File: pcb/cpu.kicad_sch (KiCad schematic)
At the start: 14 parts, among them J9 CLKMUL SET, U1 486Socket

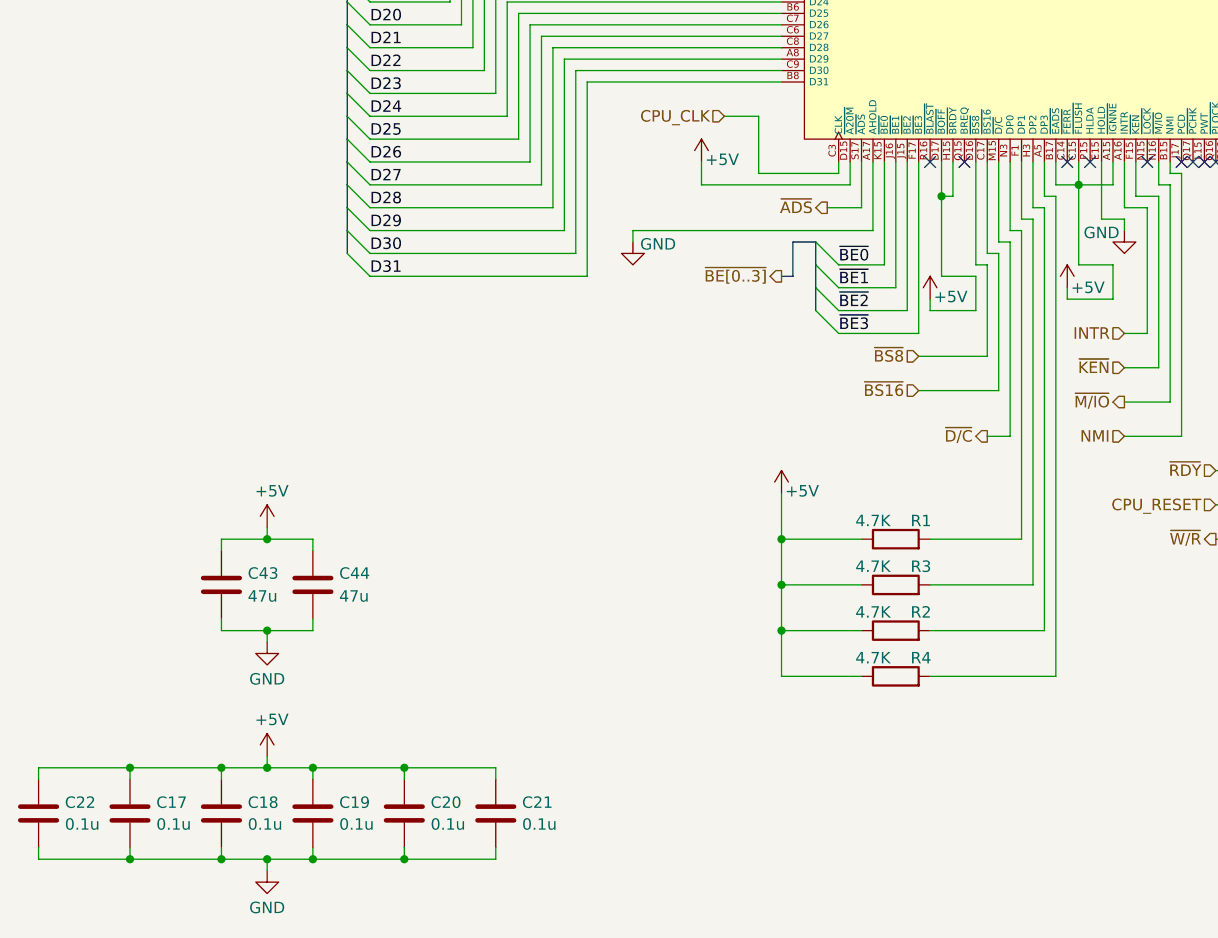
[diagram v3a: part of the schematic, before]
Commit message: cpu DPx use Resistor Array instead of individual resistors
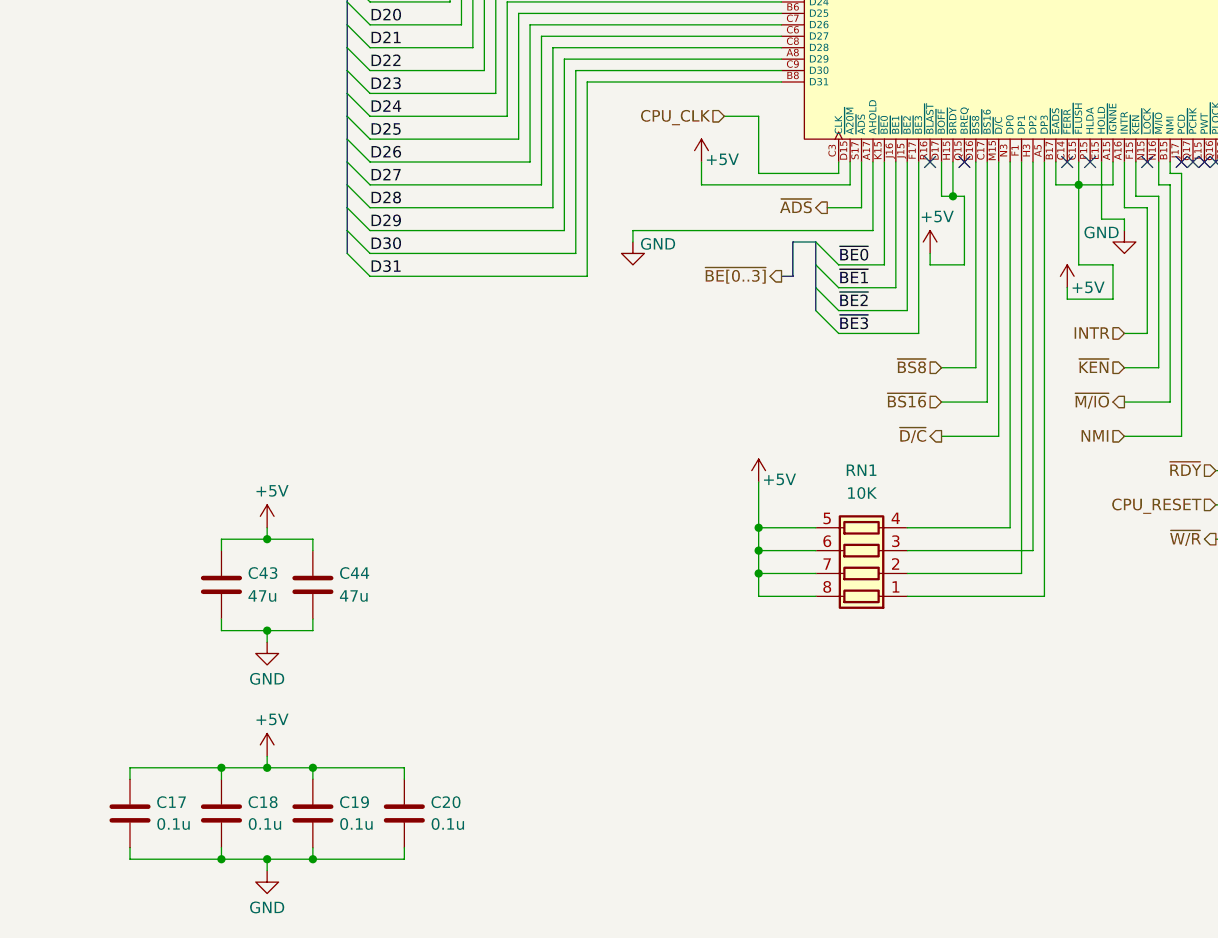
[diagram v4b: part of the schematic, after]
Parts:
- removed C21, C22: 0.1u, Capacitor_SMD:C_0805_2012Metric_Pad1.18x1.45mm_HandSolder, symbol Device:C
- removed R1, R2, R3, R4: 4.7K, Resistor_SMD:R_0805_2012Metric_Pad1.20x1.40mm_HandSolder, symbol Device:R
- added RN1: 10K, Resistor_SMD:R_Array_Convex_4x1206, symbol Device:R_Pack04
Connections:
- net +5V: now also RN1.5 (R4.2), RN1.6 (R3.2), RN1.7 (R2.2), RN1.8 (R1.2)
- net at U1.N3 (DP0): now also RN1.4 (R4.1)
- net at U1.A5 (DP3): now also RN1.1 (R1.1)
- net at U1.F1 (DP1): now also RN1.2 (R2.1)
- net at U1.H3 (DP2): now also RN1.3 (R3.1)

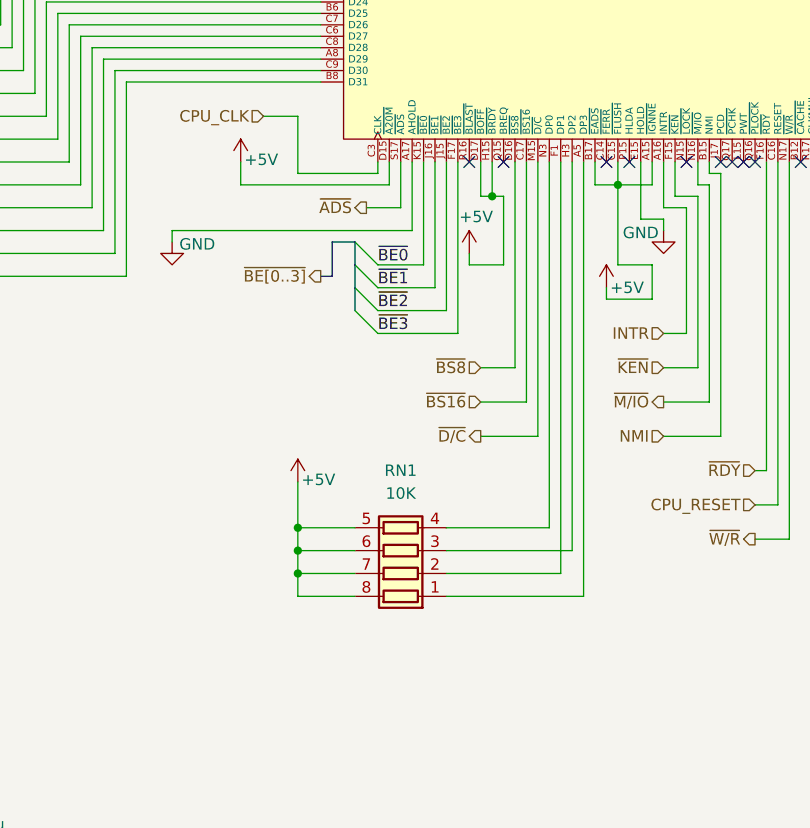
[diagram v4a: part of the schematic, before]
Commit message: cpu added convenient test point on BRDY near RDY for optional link
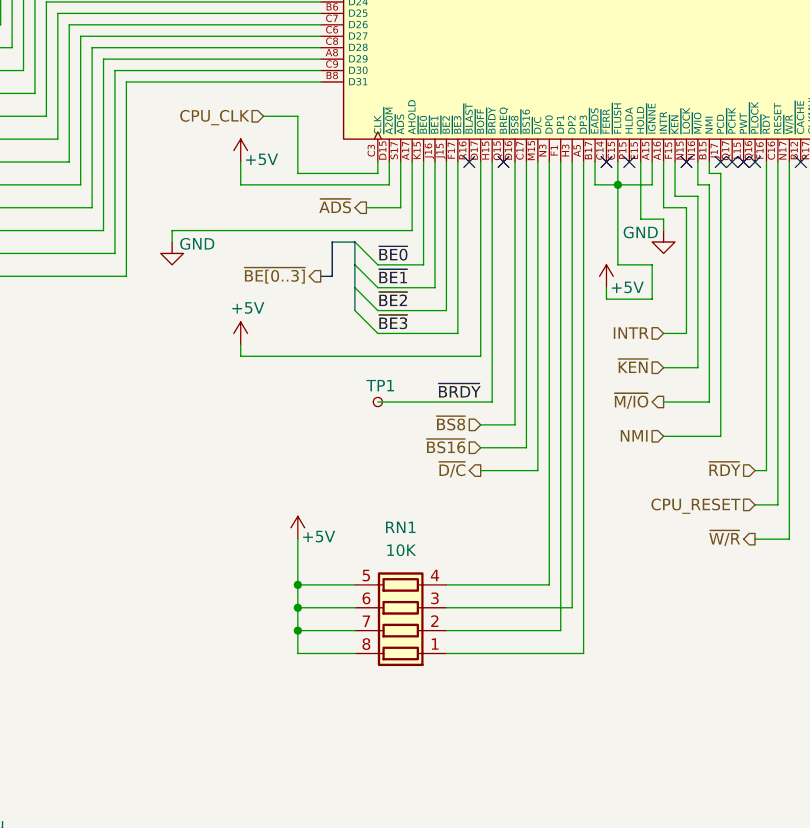
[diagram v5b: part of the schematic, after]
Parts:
- added TP1: TestPoint_Small, TestPoint:TestPoint_Pad_D1.0mm, symbol Connector:TestPoint_Small
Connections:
- net +5V: no longer U1.H15 (~{BRDY})
- new net ~{BRDY}: TP1.1, U1.H15 (~{BRDY})
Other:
- moved on the sheet: RN1

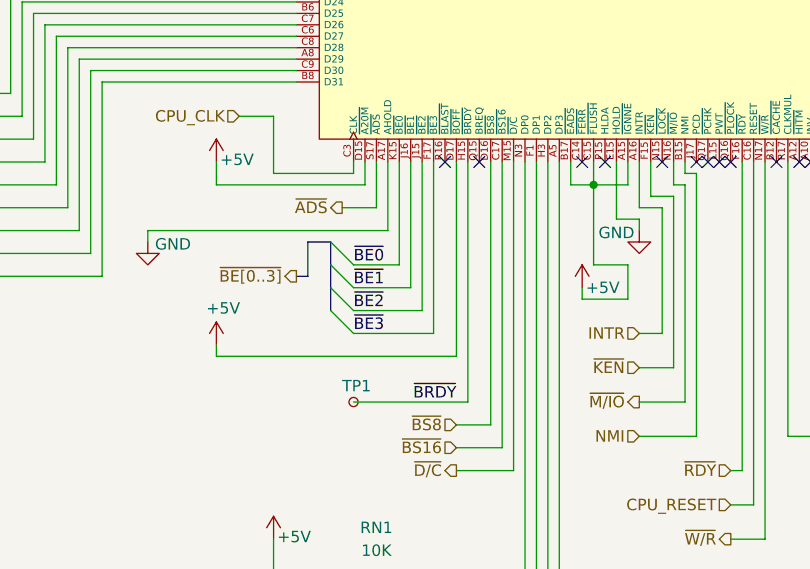
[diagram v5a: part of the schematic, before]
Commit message: reverting BRDY RDY link, wouldnt work, VIAs down to 645
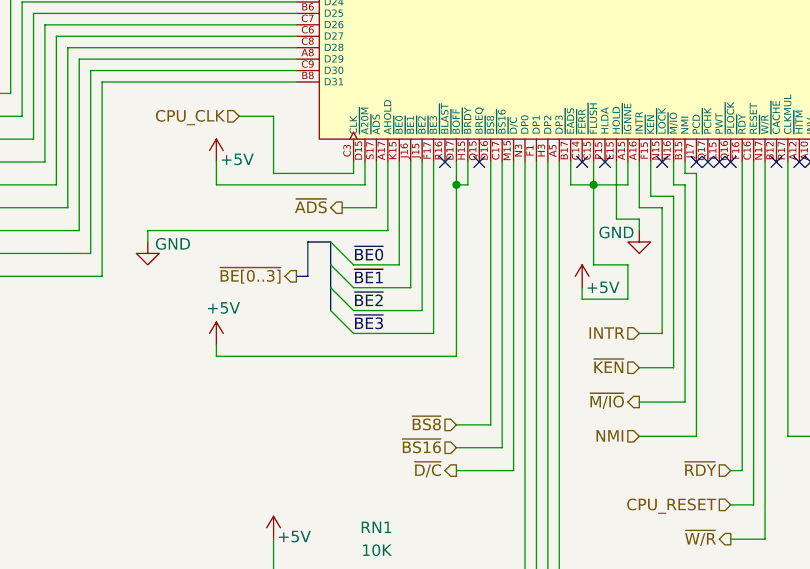
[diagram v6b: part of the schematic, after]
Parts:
- removed TP1: TestPoint_Small, TestPoint:TestPoint_Pad_D1.0mm, symbol Connector:TestPoint_Small
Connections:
- net ~{BRDY} is gone; now on net +5V: U1.H15 (~{BRDY})
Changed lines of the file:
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@@
 	)
 	(junction
+		(at 130.81 107.95)
+		(diameter 0)
+		(color 0 0 0 0)
+	)
+	(junction
 		(at 133.35 49.53)
 		(diameter 0)
@@
 	(wire
 		(pts
-			(xy 130.81 105.41) (xy 130.81 127)
+			(xy 130.81 105.41) (xy 130.81 107.95)
 		)
 		(stroke
@@
 	(wire
 		(pts
+			(xy 130.81 107.95) (xy 132.08 107.95)
+		)
+		(stroke
+			(width 0)
+			(type default)
+		)
+	)
+	(wire
+		(pts
 			(xy 127 157.48) (xy 139.7 157.48)
 		)
@@
 	(wire
 		(pts
+			(xy 130.81 107.95) (xy 130.81 127)
+		)
+		(stroke
+			(width 0)
+			(type default)
+		)
+	)
+	(wire
+		(pts
 			(xy 144.78 119.38) (xy 144.78 120.65)
 		)
@@
 	(wire
 		(pts
-			(xy 132.08 132.08) (xy 132.08 105.41)
-		)
-		(stroke
-			(width 0)
-			(type default)
-		)
-	)
-	(wire
-		(pts
 			(xy 130.81 49.53) (xy 130.81 50.8)
 		)
@@
 	(wire
 		(pts
-			(xy 119.38 132.08) (xy 132.08 132.08)
-		)
-		(stroke
-			(width 0)
-			(type default)
-		)
-	)
-	(wire
-		(pts
 			(xy 153.67 124.46) (xy 153.67 110.49)
 		)
@@
 	(wire
 		(pts
+			(xy 132.08 105.41) (xy 132.08 107.95)
+		)
+		(stroke
+			(width 0)
+			(type default)
+		)
+	)
+	(wire
+		(pts
 			(xy 140.97 105.41) (xy 140.97 154.94)
 		)
@@
 		)
 	)
-	(label "~{BRDY}"
-		(at 130.81 132.08 180)
-		(effects
-			(font
-				(size 1.27 1.27)
-			)
-			(justify right bottom)
-		)
-	)
 	(label "D20"
 		(at 67.31 90.17 0)
@@
 					(unit 1)
 				)
-			)
-		)
-	)
-	(symbol
-		(lib_id "Connector:TestPoint_Small")
-		(at 119.38 132.08 0)
-		(unit 1)
-		(exclude_from_sim no)
-		(in_bom yes)
-		(on_board yes)
-		(dnp no)
-		(property "Reference" "TP1"
-			(at 118.11 130.302 0)
-			(effects
-				(font
-					(size 1.27 1.27)
-				)
-				(justify left)
-			)
-		)
-		(property "Value" "TestPoint_Small"
-			(at 120.65 133.3499 0)
-			(effects
-				(font
-					(size 1.27 1.27)
-				)
-				(justify left)
-				(hide yes)
-			)
-		)
-		(property "Footprint" "TestPoint:TestPoint_Pad_D1.0mm"
-			(at 124.46 132.08 0)
-			(effects
-				(font
-					(size 1.27 1.27)
-				)
-				(hide yes)
-			)
-		)
-		(property "Datasheet" "~"
-			(at 124.46 132.08 0)
-			(effects
-				(font
-					(size 1.27 1.27)
-				)
-				(hide yes)
-			)
-		)
-		(property "Description" "test point"
-			(at 119.38 132.08 0)
-			(effects
-				(font
-					(size 1.27 1.27)
-				)
-				(hide yes)
-			)
-		)
-		(pin "1"
-		)
-		(instances
-			(project ""
-				(path "/360fb3b9-a21a-4226-8954-bf45cf17bb35/98e7b245-1892-4961-80dc-a2961de8ec76"
-					(reference "TP1")
-					(unit 1)
-				)
